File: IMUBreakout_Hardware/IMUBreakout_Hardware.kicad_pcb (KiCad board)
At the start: 2 copper layers, 30.5 x 25.4 mm, 11 parts, among them U1 LSM90S1

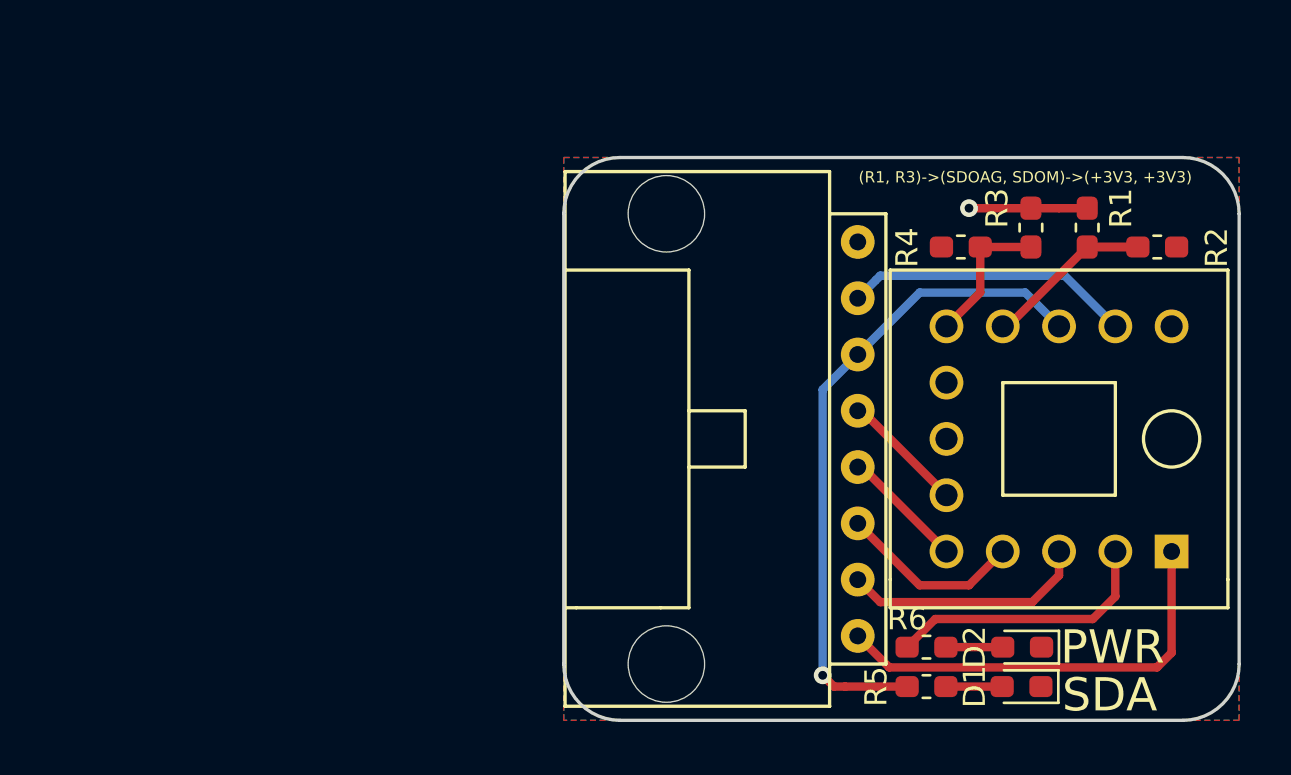
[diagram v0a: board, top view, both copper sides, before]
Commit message: Created Sparkfun Breakout
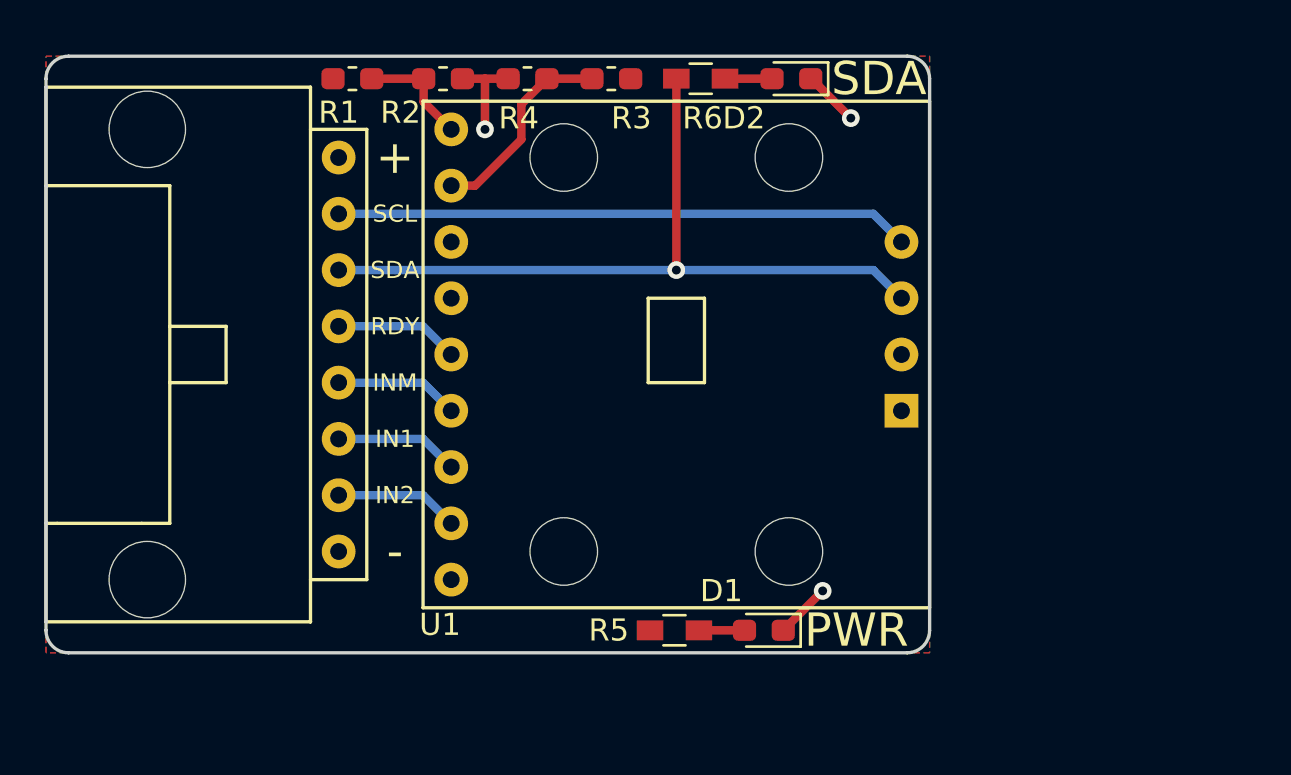
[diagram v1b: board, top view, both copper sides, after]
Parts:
- D1, D2: value D -> LED; footprint Diode_SMD:D_0603_1608Metric_Pad1.05x0.95mm_HandSolder -> LED_SMD:LED_0603_1608Metric_Pad1.05x0.95mm_HandSolder
- R5, R6: footprint Resistor_SMD:R_0603_1608Metric_Pad1.05x0.95mm_HandSolder -> Resistors_SMD:R_0603_HandSoldering
- U1: footprint MRDT_Sensors:IMU_LSM90S1 -> Packages:LSM9DS1_Sparkfun
- moved R1 33.8 mm to (125.1, 82.8), turned to 180 degrees
- moved R2 33.1 mm to (129.2, 82.8)
- moved D2 27.7 mm to (144.9, 82.8)
- moved R6 27.6 mm to (140.8, 82.8)
- moved U1 24.2 mm to (129.5, 105.4), turned to 180 degrees
- moved Conn1 23.7 mm to (124.5, 95.2)
- moved G*** 21.9 mm to (137.9, 95.2), turned to 180 degrees
- moved R4 21.0 mm to (133.0, 82.8)
- moved R3 20.1 mm to (136.8, 82.8), turned to 0 degrees
- moved D1 11.9 mm to (143.7, 107.7)
- moved R5 11.7 mm to (139.6, 107.7)
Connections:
- R5 pad 1: SDA -> +3V3
- R6 pad 1: +3V3 -> SDA
- U1 pad 1: +3V3 -> SDOAG
- U1 pad 10: INT1AG -> SCL
- U1 pad 11: INT2AG -> SDA
- U1 pad 2: SCL -> SDOM
- U1 pad 3: SDA -> +3V3
- U1 pad 4: SDOAG -> +3V3
- U1 pad 5: SDOM -> DRDYM
- U1 pad 6: +3V3 -> INTM
- U1 pad 7: +3V3 -> INT1AG
- U1 pad 8: DRDYM -> INT2AG
- U1 pad 9: INTM -> +3V3
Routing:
- net +3V3: track 17.7 -> 0.00 mm, vias 1 -> 0
- net SCL: track 13.0 -> 25.9 mm
- net GND: track 19.6 -> 9.40 mm, vias 0 -> 3
- net INT2AG: track 11.1 -> 5.61 mm
- net SDA: track 30.0 -> 34.6 mm
- net SDOAG: track 9.61 -> 5.14 mm
- net SDOM: track 6.50 -> 9.79 mm
- net INT1AG: track 8.33 -> 5.61 mm
- added copper zone on F.Cu, net +3V3
- added copper zone on B.Cu, net GND
- removed copper zone on B.Cu, net +3V3
- removed copper zone on F.Cu, net GND
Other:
- board size 30.5 x 25.4 mm -> 39.9 x 26.9 mm
- board text added: "+"
- board text added: "-"
- board text added: "IMU Breakout Mars Rover Design Team Missouri S&T, 2019 Andrew Van Horn"
- board text added: "IN1"
- board text added: "IN2"
- board text added: "INM"
- board text added: "RDY"
- board text added: "SCL"
- board text removed: "(R1, R3)->(SDOAG, SDOM)->(+3V3, +3V3)"
- board text removed: "IMU Breakout, Rev 1 Mars Rover, 2019 Missouri S&T"
